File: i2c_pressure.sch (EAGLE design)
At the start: 4 parts, among them IC1 TCAN1051HGV, U1 SSCDANT030PASA5, U2 SSCDANT030PASA5, U3 SSCDANT030PASA5

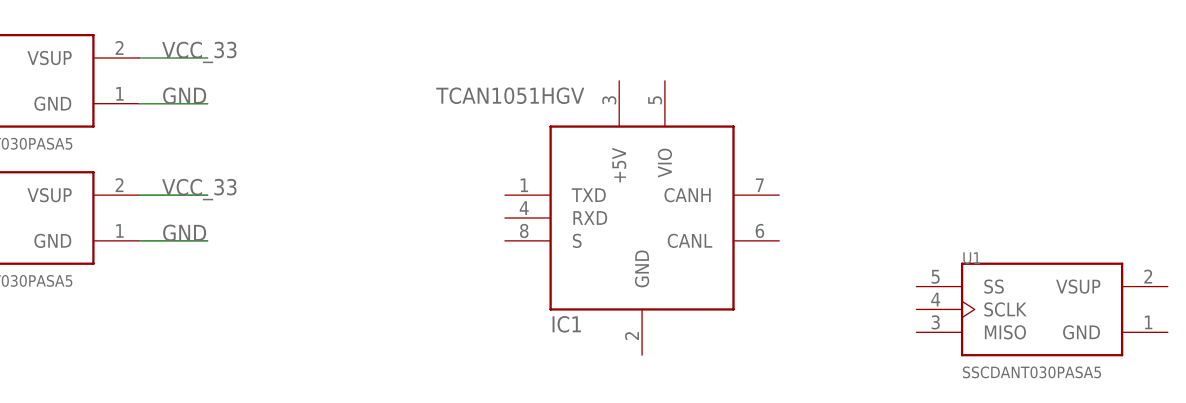
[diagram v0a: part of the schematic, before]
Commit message: pressure board needs i2c mux, introduce engmon-wroom
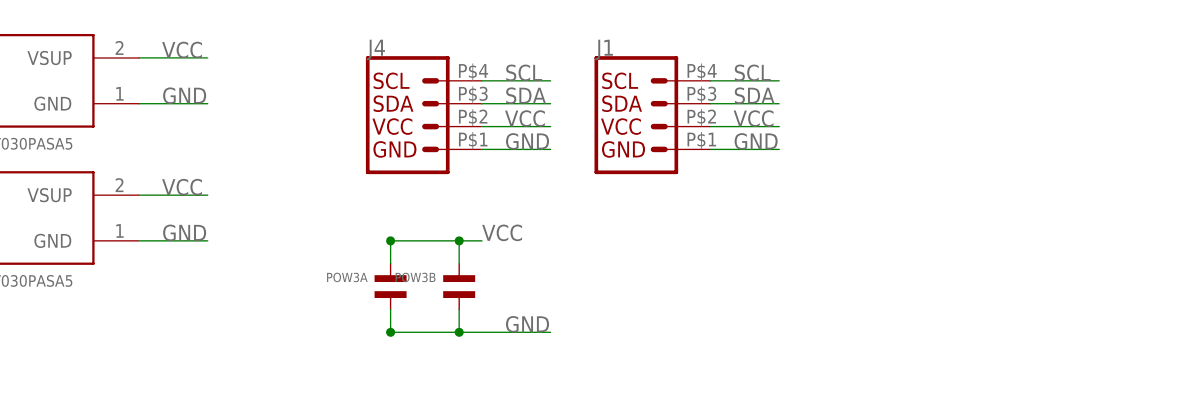
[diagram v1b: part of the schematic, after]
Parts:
- removed IC1: TCAN1051HGV, microbuilder:CAN_TRANSCIEVER_TCAN1051V
- removed U1: SSCDANT030PASA5, SSCDANT030PASA5:SSCDANT030PASA5
- added J1, J4: Vertical Qwiic Connector, 00jim:QWIIC_CONNECTORJST04_1MM_HOLE
- added POW3A, POW3B: (no value), MF_Passives:CAPACITOR_NP_0603
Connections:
- removed net VCC_33: U2.VSUP, U3.VSUP
- new net VCC: J1.2, J4.2, POW3A.P$1, POW3B.P$1, U2.VSUP, U3.VSUP
- net GND: now also J1.1, J4.1, POW3A.P$2, POW3B.P$2
- net SCL: now also J1.4, J4.4
- net SDA: now also J1.3, J4.3
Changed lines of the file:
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@@
 <class number="0" name="default" width="0.254" drill="0">
+</class>
+<class number="3" name="hc" width="0.508" drill="0">
 </class>
 </classes>
 <parts>
-<part name="IC1" library="microbuilder" deviceset="CAN_TRANSCIEVER" device="_TCAN1051V" value="TCAN1051HGV"/>
-<part name="U1" library="SSCDANT030PASA5" deviceset="SSCDANT030PASA5" device=""/>
 <part name="U2" library="SSCDANT030PASA5" deviceset="SSCDANT030PASA5" device=""/>
 <part name="U3" library="SSCDANT030PASA5" deviceset="SSCDANT030PASA5" device=""/>
+<part name="J4" library="00jim" deviceset="QWIIC_CONNECTOR" device="JST04_1MM_HOLE" value="Vertical Qwiic Connector"/>
+<part name="POW3B" library="MF_Passives" deviceset="CAPACITOR_NP" device="_0603"/>
+<part name="POW3A" library="MF_Passives" deviceset="CAPACITOR_NP" device="_0603"/>
+<part name="J1" library="00jim" deviceset="QWIIC_CONNECTOR" device="JST04_1MM_HOLE" value="Vertical Qwiic Connector"/>
 </parts>
 <sheets>
@@
 </plain>
 <instances>
-<instance part="IC1" gate="G$1" x="109.22" y="60.96" smashed="yes">
-<attribute name="NAME" x="99.06" y="48.26" size="1.778" layer="95"/>
-<attribute name="VALUE" x="86.36" y="73.66" size="1.778" layer="96"/>
-</instance>
-<instance part="U1" gate="G$1" x="154.94" y="50.8" smashed="yes">
-<attribute name="NAME" x="144.7783" y="55.880840625" size="1.270209375" layer="95"/>
-<attribute name="VALUE" x="144.7713" y="43.173459375" size="1.271090625" layer="96"/>
-</instance>
 <instance part="U2" gate="G$1" x="40.64" y="76.2" smashed="yes">
 <attribute name="NAME" x="30.4783" y="81.280840625" size="1.270209375" layer="95"/>
@@
 <attribute name="NAME" x="30.4783" y="66.040840625" size="1.270209375" layer="95"/>
 <attribute name="VALUE" x="30.4713" y="53.333459375" size="1.271090625" layer="96"/>
+</instance>
+<instance part="J4" gate="G$1" x="83.82" y="71.12" smashed="yes">
+<attribute name="NAME" x="78.74" y="78.994" size="1.778" layer="95" font="vector"/>
+</instance>
+<instance part="POW3B" gate="G$1" x="88.9" y="53.34" smashed="yes" rot="MR0">
+<attribute name="NAME" x="86.36" y="54.864" size="1.016" layer="95" font="vector" rot="MR0" align="top-left"/>
+<attribute name="VALUE" x="86.36" y="51.816" size="1.016" layer="96" font="vector" rot="MR0"/>
+</instance>
+<instance part="POW3A" gate="G$1" x="81.28" y="53.34" smashed="yes" rot="MR0">
+<attribute name="NAME" x="78.74" y="54.864" size="1.016" layer="95" font="vector" rot="MR0" align="top-left"/>
+<attribute name="VALUE" x="78.74" y="51.816" size="1.016" layer="96" font="vector" rot="MR0"/>
+</instance>
+<instance part="J1" gate="G$1" x="109.22" y="71.12" smashed="yes">
+<attribute name="NAME" x="104.14" y="78.994" size="1.778" layer="95" font="vector"/>
 </instance>
 </instances>
@@
 <label x="55.88" y="58.42" size="1.778" layer="95"/>
 </segment>
+<segment>
+<wire x1="91.44" y1="68.58" x2="99.06" y2="68.58" width="0.1524" layer="91"/>
+<label x="93.98" y="68.58" size="1.778" layer="95"/>
+<pinref part="J4" gate="G$1" pin="1"/>
+</segment>
+<segment>
+<pinref part="POW3B" gate="G$1" pin="P$2"/>
+<wire x1="88.9" y1="50.8" x2="88.9" y2="48.26" width="0.2032" layer="91"/>
+<wire x1="99.06" y1="48.26" x2="88.9" y2="48.26" width="0.1524" layer="91"/>
+<wire x1="88.9" y1="48.26" x2="81.28" y2="48.26" width="0.1524" layer="91"/>
+<junction x="88.9" y="48.26"/>
+<wire x1="81.28" y1="48.26" x2="81.28" y2="50.8" width="0.1524" layer="91"/>
+<pinref part="POW3A" gate="G$1" pin="P$2"/>
+<junction x="81.28" y="48.26"/>
+<label x="93.98" y="48.26" size="1.778" layer="95"/>
+</segment>
+<segment>
+<wire x1="116.84" y1="68.58" x2="124.46" y2="68.58" width="0.1524" layer="91"/>
+<label x="119.38" y="68.58" size="1.778" layer="95"/>
+<pinref part="J1" gate="G$1" pin="1"/>
+</segment>
 </net>
 <net name="SDA" class="0">
@@
 <wire x1="25.4" y1="58.42" x2="17.78" y2="58.42" width="0.1524" layer="91"/>
 <label x="17.78" y="58.42" size="1.778" layer="95"/>
+</segment>
+<segment>
+<wire x1="91.44" y1="73.66" x2="99.06" y2="73.66" width="0.1524" layer="91"/>
+<label x="93.98" y="73.66" size="1.778" layer="95"/>
+<pinref part="J4" gate="G$1" pin="3"/>
+</segment>
+<segment>
+<wire x1="116.84" y1="73.66" x2="124.46" y2="73.66" width="0.1524" layer="91"/>
+<label x="119.38" y="73.66" size="1.778" layer="95"/>
+<pinref part="J1" gate="G$1" pin="3"/>
 </segment>
 </net>
@@
 <label x="17.78" y="60.96" size="1.778" layer="95"/>
 </segment>
+<segment>
+<wire x1="91.44" y1="76.2" x2="99.06" y2="76.2" width="0.1524" layer="91"/>
+<label x="93.98" y="76.2" size="1.778" layer="95"/>
+<pinref part="J4" gate="G$1" pin="4"/>
+</segment>
+<segment>
+<wire x1="116.84" y1="76.2" x2="124.46" y2="76.2" width="0.1524" layer="91"/>
+<label x="119.38" y="76.2" size="1.778" layer="95"/>
+<pinref part="J1" gate="G$1" pin="4"/>
+</segment>
 </net>
-<net name="VCC_33" class="0">
+<net name="VCC" class="0">
+<segment>
+<wire x1="91.44" y1="71.12" x2="99.06" y2="71.12" width="0.1524" layer="91"/>
+<label x="93.98" y="71.12" size="1.778" layer="95"/>
+<pinref part="J4" gate="G$1" pin="2"/>
+</segment>
 <segment>
 <pinref part="U2" gate="G$1" pin="VSUP"/>
@@
 <label x="55.88" y="63.5" size="1.778" layer="95"/>
 </segment>
+<segment>
+<wire x1="91.44" y1="58.42" x2="88.9" y2="58.42" width="0.2032" layer="91"/>
+<pinref part="POW3B" gate="G$1" pin="P$1"/>
+<wire x1="88.9" y1="55.88" x2="88.9" y2="58.42" width="0.1524" layer="91"/>
+<wire x1="88.9" y1="58.42" x2="81.28" y2="58.42" width="0.1524" layer="91"/>
+<junction x="88.9" y="58.42"/>
+<wire x1="81.28" y1="58.42" x2="81.28" y2="55.88" width="0.1524" layer="91"/>
+<pinref part="POW3A" gate="G$1" pin="P$1"/>
+<junction x="81.28" y="58.42"/>
+<label x="91.44" y="58.42" size="1.778" layer="95"/>
+</segment>
+<segment>
+<wire x1="116.84" y1="71.12" x2="124.46" y2="71.12" width="0.1524" layer="91"/>
+<label x="119.38" y="71.12" size="1.778" layer="95"/>
+<pinref part="J1" gate="G$1" pin="2"/>
+</segment>
 </net>
